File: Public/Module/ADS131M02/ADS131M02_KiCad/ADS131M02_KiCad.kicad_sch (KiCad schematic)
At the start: 8 parts, among them U1 ADS131M02_TSSOP20, U2 LP2985-3.3

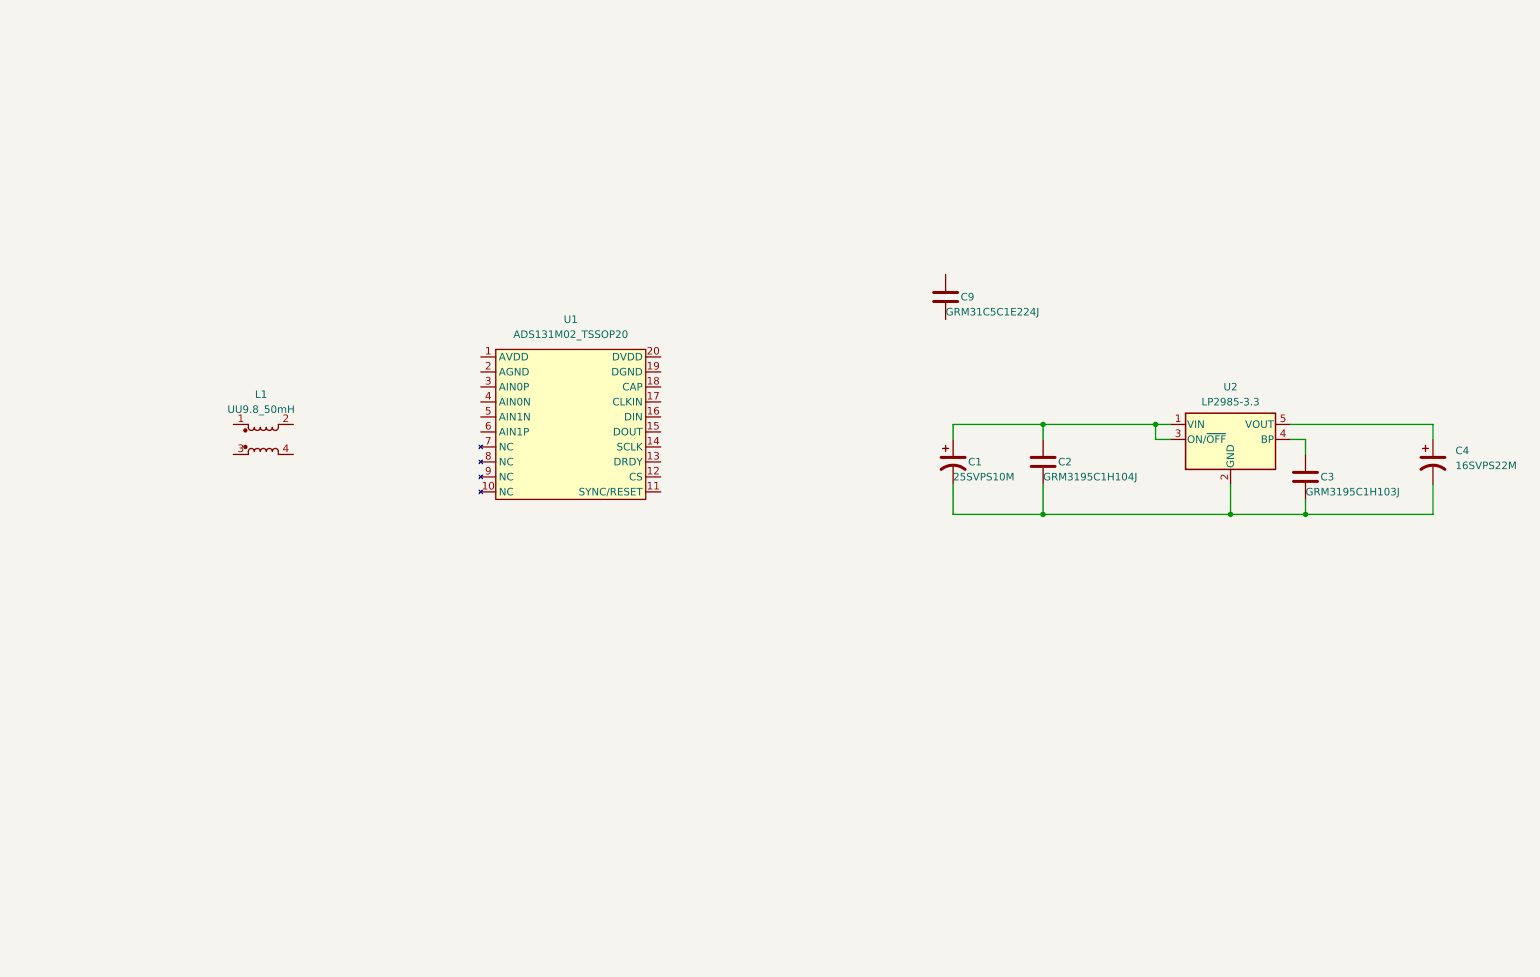
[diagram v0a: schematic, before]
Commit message: Update ADS131M02 Module
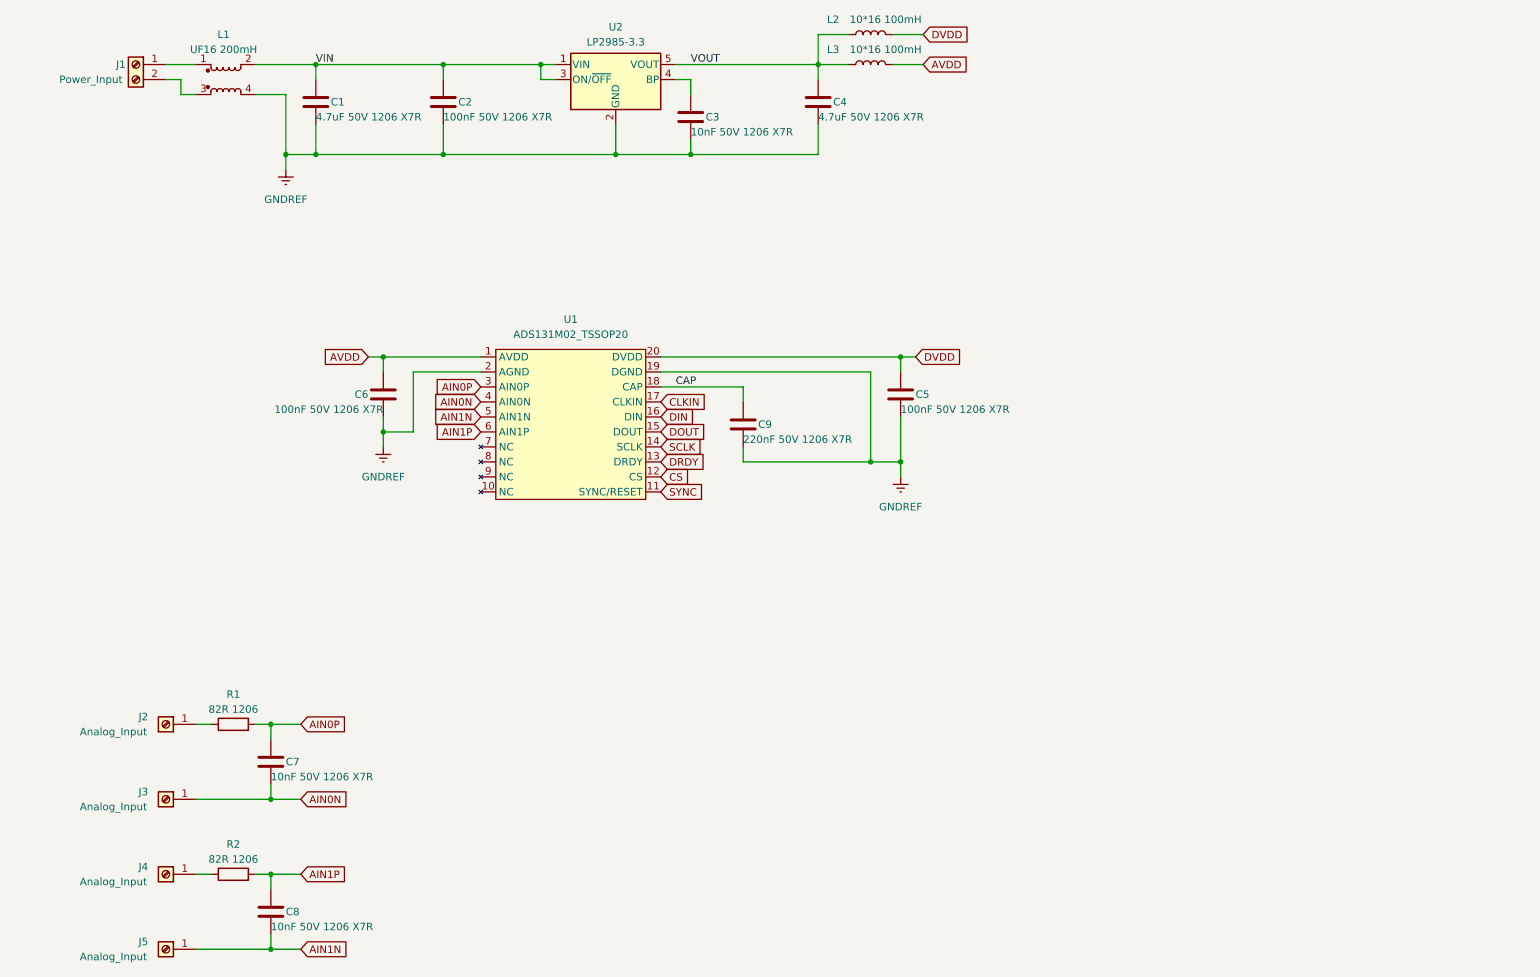
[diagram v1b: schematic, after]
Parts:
- removed C1: 25SVPS10M, symbol Device:C_Polarized_US
- removed C4: 16SVPS22M, symbol Device:C_Polarized_US
- added C1, C4: 4.7uF 50V 1206 X7R, Capacitor_SMD:C_1206_3216Metric, symbol Device:C
- added C5, C6: 100nF 50V 1206 X7R, Capacitor_SMD:C_1206_3216Metric, symbol Device:C
- added C7, C8: 10nF 50V 1206 X7R, Capacitor_SMD:C_1206_3216Metric, symbol Device:C
- added J1: Power_Input, Customer_Connector:2EDG-5.08mm_2P_Horizontal, symbol Connector:Screw_Terminal_01x02
- added J2, J3, J4, J5: Analog_Input, Customer_Connector:AMASS_24.245, symbol Connector:Screw_Terminal_01x01
- added L2, L3: 10*16 100mH, symbol Device:L
- added R1, R2: 82R 1206, Resistor_SMD:R_1206_3216Metric, symbol Device:R
- C2: value GRM3195C1H104J -> 100nF 50V 1206 X7R; footprint (none) -> Capacitor_SMD:C_1206_3216Metric
- C3: value GRM3195C1H103J -> 10nF 50V 1206 X7R; footprint (none) -> Capacitor_SMD:C_1206_3216Metric
- C9: value GRM31C5C1E224J -> 220nF 50V 1206 X7R; footprint (none) -> Capacitor_SMD:C_1206_3216Metric
- L1: value UU9.8_50mH -> UF16 200mH
- U1: footprint (none) -> Package_SO:TSSOP-20_4.4x6.5mm_P0.65mm
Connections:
- net VIN: now reaches C2.1, U2.1 (VIN), U2.3 (ON/~{OFF})
- net VIN: now also L1.2, C1.1
- net GNDREF: now reaches C2.2, C3.2, U2.2 (GND)
- net GNDREF: now also C9.2, L1.4, U1.19 (DGND), U1.2 (AGND), C1.2, C4.2, C5.2, C6.2
- net VOUT: now reaches U2.5 (VOUT)
- net VOUT: now also C4.1, L2.1, L3.1
- net at L1.1: now also J1.1 (Pin_1)
- net at L1.3: now also J1.2 (Pin_2)
- net AVDD: now reaches U1.1 (AVDD)
- net AVDD: now also C6.1, L3.2
- net SYNC: now reaches U1.11 (SYNC/RESET)
- net CS: now reaches U1.12 (CS)
- net DRDY: now reaches U1.13 (DRDY)
- net SCLK: now reaches U1.14 (SCLK)
- net DOUT: now reaches U1.15 (DOUT)
- net DIN: now reaches U1.16 (DIN)
- net CLKIN: now reaches U1.17 (CLKIN)
- net CAP: now reaches U1.18 (CAP)
- net CAP: now also C9.1
- net DVDD: now reaches U1.20 (DVDD)
- net DVDD: now also C5.1, L2.2
- net AIN0P: now reaches U1.3 (AIN0P)
- net AIN0P: now also C7.1, R1.2
- net AIN0N: now reaches U1.4 (AIN0N)
- net AIN0N: now also C7.2, J3.1 (Pin_1)
- net AIN1N: now reaches U1.5 (AIN1N)
- net AIN1N: now also C8.2, J5.1 (Pin_1)
- net AIN1P: now reaches U1.6 (AIN1P)
- net AIN1P: now also C8.1, R2.2
- new net: J2.1 (Pin_1), R1.1
- new net: J4.1 (Pin_1), R2.1
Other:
- moved on the sheet: C2, C3, C9, L1, U2

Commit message: Update ADS131M02 Module
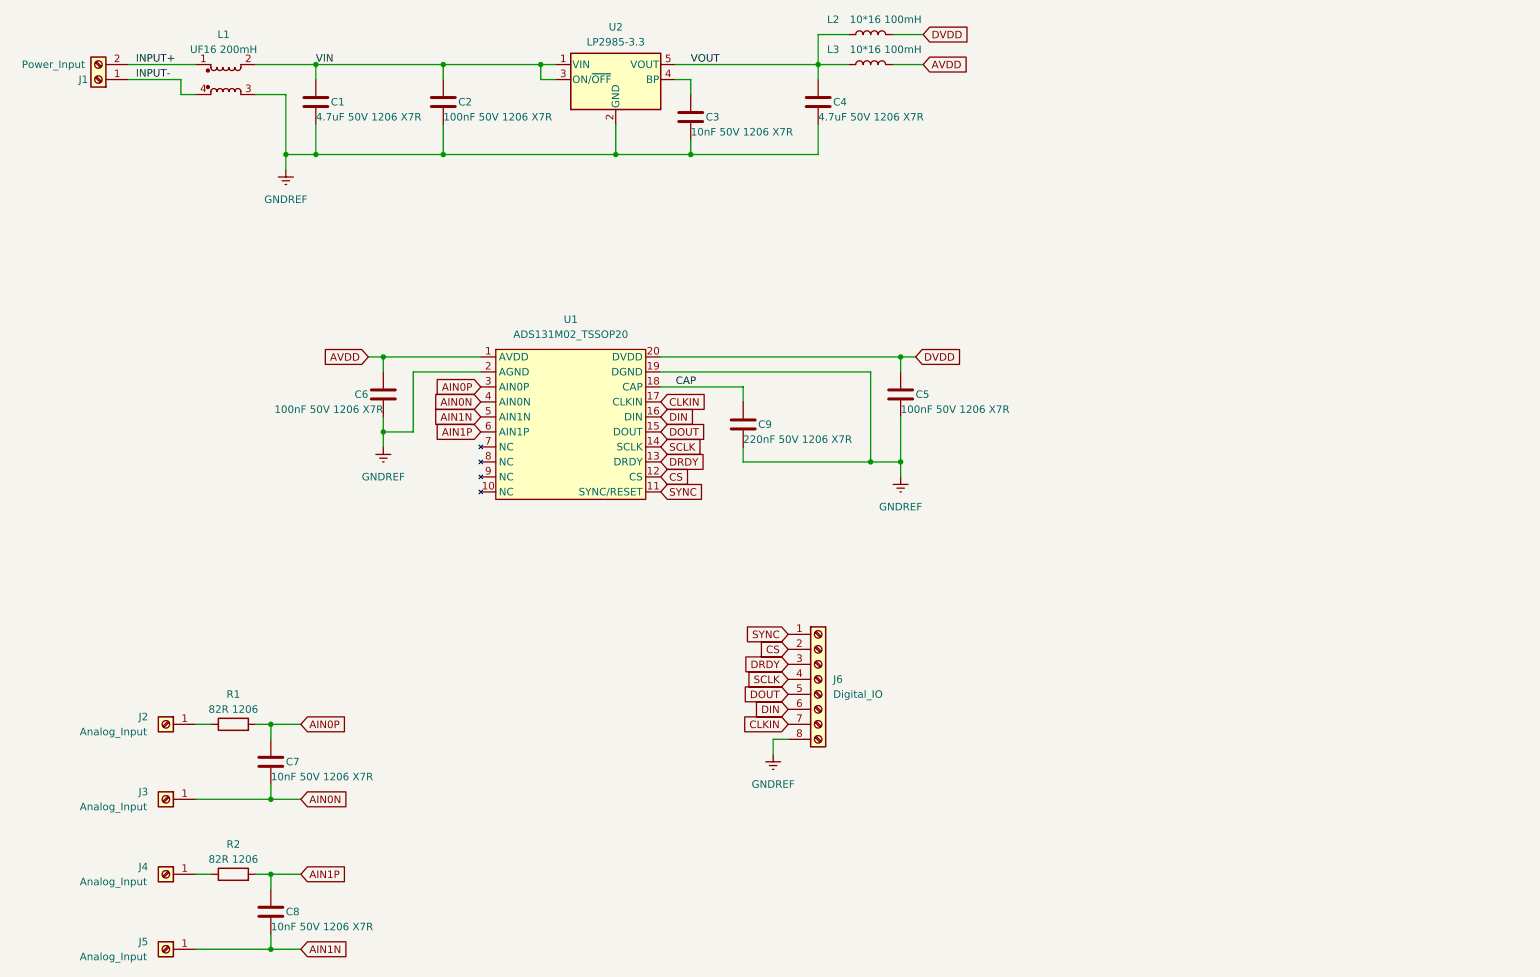
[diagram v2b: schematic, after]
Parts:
- added J6: Digital_IO, Customer_Connector:2EDG-5.08mm_8P_Horizontal, symbol Connector:Screw_Terminal_01x08
- L1: footprint (none) -> Customer_Passive:Inductor_Coupled_THT_UF16; symbol Device:L_Coupled -> Device:L_Coupled_1243
- L2, L3: footprint (none) -> Customer_Passive:Inductor_THT_10x16
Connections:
- net CLKIN: now also J6.7 (Pin_7)
- net CS: now also J6.2 (Pin_2)
- net DIN: now also J6.6 (Pin_6)
- net DOUT: now also J6.5 (Pin_5)
- net DRDY: now also J6.3 (Pin_3)
- net GNDREF: now also L1.3, J6.8 (Pin_8); no longer L1.4
- net SCLK: now also J6.4 (Pin_4)
- net SYNC: now also J6.1 (Pin_1)
- net INPUT+: now reaches L1.1
- net INPUT+: now also J1.2 (Pin_2); no longer J1.1 (Pin_1)
- new net INPUT-: J1.1 (Pin_1), L1.4
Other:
- moved on the sheet: J1
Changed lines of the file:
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@@
+    (stroke (width 0) (type default))
+  )
+  (wire (pts (xy 148.59 144.78) (xy 148.59 142.24))
     (stroke (width 0) (type default))
   )
@@
     (stroke (width 0) (type default))
   )
-  (wire (pts (xy 45.72 27.94) (xy 50.8 27.94))
+  (wire (pts (xy 39.37 27.94) (xy 50.8 27.94))
     (stroke (width 0) (type default))
   )
@@
     (stroke (width 0) (type default))
   )
+  (wire (pts (xy 148.59 142.24) (xy 151.13 142.24))
+    (stroke (width 0) (type default))
+  )
   (wire (pts (xy 143.51 92.71) (xy 143.51 95.25))
     (stroke (width 0) (type default))
@@
     (stroke (width 0) (type default))
   )
-  (wire (pts (xy 45.72 30.48) (xy 48.26 30.48))
+  (wire (pts (xy 39.37 30.48) (xy 48.26 30.48))
     (stroke (width 0) (type default))
   )
@@
   (wire (pts (xy 92.71 43.18) (xy 121.92 43.18))
     (stroke (width 0) (type default))
+  )
+  (label "INPUT-" (at 40.64 30.48 0) (fields_autoplaced)
+    (effects (font (size 1.27 1.27)) (justify left bottom))
   )
   (label "CAP" (at 132.08 82.55 0) (fields_autoplaced)
     (effects (font (size 1.27 1.27)) (justify left bottom))
   )
+  (label "INPUT+" (at 40.64 27.94 0) (fields_autoplaced)
+    (effects (font (size 1.27 1.27)) (justify left bottom))
+  )
   (label "VOUT" (at 134.62 27.94 0) (fields_autoplaced)
     (effects (font (size 1.27 1.27)) (justify left bottom))
@@
     )
   )
+  (global_label "DRDY" (shape input) (at 151.13 129.54 180) (fields_autoplaced)
+    (effects (font (size 1.27 1.27)) (justify right))
+    (property "Intersheetrefs" "${INTERSHEET_REFS}" (at 143.2462 129.54 0)
+      (effects (font (size 1.27 1.27)) (justify right) hide)
+    )
+  )
   (global_label "DVDD" (shape input) (at 173.99 22.86 0) (fields_autoplaced)
     (effects (font (size 1.27 1.27)) (justify left))
@@
     )
   )
+  (global_label "SCLK" (shape input) (at 151.13 132.08 180) (fields_autoplaced)
+    (effects (font (size 1.27 1.27)) (justify right))
+    (property "Intersheetrefs" "${INTERSHEET_REFS}" (at 143.3672 132.08 0)
+      (effects (font (size 1.27 1.27)) (justify right) hide)
+    )
+  )
   (global_label "AIN1P" (shape input) (at 68.58 165.1 0) (fields_autoplaced)
     (effects (font (size 1.27 1.27)) (justify left))
@@
     )
   )
+  (global_label "CS" (shape input) (at 151.13 127 180) (fields_autoplaced)
+    (effects (font (size 1.27 1.27)) (justify right))
+    (property "Intersheetrefs" "${INTERSHEET_REFS}" (at 145.6653 127 0)
+      (effects (font (size 1.27 1.27)) (justify right) hide)
+    )
+  )
   (global_label "CLKIN" (shape input) (at 129.54 85.09 0) (fields_autoplaced)
     (effects (font (size 1.27 1.27)) (justify left))
@@
     )
   )
+  (global_label "DIN" (shape input) (at 151.13 137.16 180) (fields_autoplaced)
+    (effects (font (size 1.27 1.27)) (justify right))
+    (property "Intersheetrefs" "${INTERSHEET_REFS}" (at 144.9395 137.16 0)
+      (effects (font (size 1.27 1.27)) (justify right) hide)
+    )
+  )
+  (global_label "DOUT" (shape input) (at 151.13 134.62 180) (fields_autoplaced)
+    (effects (font (size 1.27 1.27)) (justify right))
+    (property "Intersheetrefs" "${INTERSHEET_REFS}" (at 143.2462 134.62 0)
+      (effects (font (size 1.27 1.27)) (justify right) hide)
+    )
+  )
+  (global_label "SYNC" (shape input) (at 151.13 124.46 180) (fields_autoplaced)
+    (effects (font (size 1.27 1.27)) (justify right))
+    (property "Intersheetrefs" "${INTERSHEET_REFS}" (at 143.2462 124.46 0)
+      (effects (font (size 1.27 1.27)) (justify right) hide)
+    )
+  )
   (global_label "DVDD" (shape input) (at 172.72 77.47 0) (fields_autoplaced)
     (effects (font (size 1.27 1.27)) (justify left))
@@
     )
   )
+  (global_label "CLKIN" (shape input) (at 151.13 139.7 180) (fields_autoplaced)
+    (effects (font (size 1.27 1.27)) (justify right))
+    (property "Intersheetrefs" "${INTERSHEET_REFS}" (at 142.6414 139.7 0)
+      (effects (font (size 1.27 1.27)) (justify right) hide)
+    )
+  )
   (symbol (lib_id "Connector:Screw_Terminal_01x01") (at 45.72 177.8 0) (mirror y) (unit 1)
     (in_bom yes) (on_board yes) (dnp no)
@@
       (effects (font (size 1.27 1.27)))
     )
-    (property "Footprint" "" (at 165.1 22.86 0)
+    (property "Footprint" "Customer_Passive:Inductor_THT_10x16" (at 165.1 22.86 0)
       (effects (font (size 1.27 1.27)) hide)
     )
@@
     )
   )
-  (symbol (lib_id "Connector:Screw_Terminal_01x02") (at 40.64 27.94 0) (mirror y) (unit 1)
-    (in_bom yes) (on_board yes) (dnp no)
-    (property "Reference" "J1" (at 38.1 27.94 0)
-      (effects (font (size 1.27 1.27)))
-    )
-    (property "Value" "Power_Input" (at 33.02 30.48 0)
-      (effects (font (size 1.27 1.27)))
-    )
-    (property "Footprint" "Customer_Connector:2EDG-5.08mm_2P_Horizontal" (at 40.64 27.94 0)
-      (effects (font (size 1.27 1.27)) hide)
-    )
-    (property "Datasheet" "~" (at 40.64 27.94 0)
+  (symbol (lib_id "Connector:Screw_Terminal_01x02") (at 34.29 30.48 180) (unit 1)
+    (in_bom yes) (on_board yes) (dnp no)
+    (property "Reference" "J1" (at 31.75 30.48 0)
+      (effects (font (size 1.27 1.27)))
+    )
+    (property "Value" "Power_Input" (at 26.67 27.94 0)
+      (effects (font (size 1.27 1.27)))
+    )
+    (property "Footprint" "Customer_Connector:2EDG-5.08mm_2P_Horizontal" (at 34.29 30.48 0)
+      (effects (font (size 1.27 1.27)) hide)
+    )
+    (property "Datasheet" "~" (at 34.29 30.48 0)
       (effects (font (size 1.27 1.27)) hide)
     )
@@
     )
   )
-  (symbol (lib_id "Device:L_Coupled") (at 55.88 30.48 0) (unit 1)
-    (in_bom yes) (on_board yes) (dnp no) (fields_autoplaced)
+  (symbol (lib_id "Device:L_Coupled_1243") (at 55.88 30.48 0) (unit 1)
+    (in_bom yes) (on_board yes) (dnp no)
     (property "Reference" "L1" (at 55.499 22.86 0)
       (effects (font (size 1.27 1.27)))
@@
       (effects (font (size 1.27 1.27)))
     )
-    (property "Footprint" "" (at 55.88 30.48 0)
+    (property "Footprint" "Customer_Passive:Inductor_Coupled_THT_UF16" (at 55.88 30.48 0)
       (effects (font (size 1.27 1.27)) hide)
     )
@@
     )
   )
+  (symbol (lib_id "Connector:Screw_Terminal_01x08") (at 156.21 132.08 0) (unit 1)
+    (in_bom yes) (on_board yes) (dnp no) (fields_autoplaced)
+    (property "Reference" "J6" (at 158.75 132.08 0)
+      (effects (font (size 1.27 1.27)) (justify left))
+    )
+    (property "Value" "Digital_IO" (at 158.75 134.62 0)
+      (effects (font (size 1.27 1.27)) (justify left))
+    )
+    (property "Footprint" "Customer_Connector:2EDG-5.08mm_8P_Horizontal" (at 156.21 132.08 0)
+      (effects (font (size 1.27 1.27)) hide)
+    )
+    (property "Datasheet" "~" (at 156.21 132.08 0)
+      (effects (font (size 1.27 1.27)) hide)
+    )
+    (pin "1")
+    (pin "2")
+    (pin "3")
+    (pin "4")
+    (pin "5")
+    (pin "6")
+    (pin "7")
+    (pin "8")
+    (instances
+      (project "ADS131M02_KiCad"
+        (path "/7d2fbb59-57e0-429a-94f3-b0f859024267"
+          (reference "J6") (unit 1)
+        )
+      )
+    )
+  )
   (symbol (lib_id "Device:C") (at 143.51 88.9 0) (unit 1)
     (in_bom yes) (on_board yes) (dnp no)
@@
       (effects (font (size 1.27 1.27)))
     )
-    (property "Footprint" "" (at 165.1 27.94 0)
+    (property "Footprint" "Customer_Passive:Inductor_THT_10x16" (at 165.1 27.94 0)
       (effects (font (size 1.27 1.27)) hide)
     )
@@
         )
       )
+    )
+  )
+  (symbol (lib_id "power:GNDREF") (at 148.59 144.78 0) (unit 1)
+    (in_bom yes) (on_board yes) (dnp no) (fields_autoplaced)
+    (property "Reference" "#PWR04" (at 148.59 151.13 0)
+      (effects (font (size 1.27 1.27)) hide)
+    )
+    (property "Value" "GNDREF" (at 148.59 149.86 0)
+      (effects (font (size 1.27 1.27)))
+    )
+    (property "Footprint" "" (at 148.59 144.78 0)
+      (effects (font (size 1.27 1.27)) hide)
+    )
+    (property "Datasheet" "" (at 148.59 144.78 0)
+      (effects (font (size 1.27 1.27)) hide)
+    )
+    (pin "1")
+    (instances
+      (project "ADS131M02_KiCad"
+        (path "/7d2fbb59-57e0-429a-94f3-b0f859024267"
+          (reference "#PWR04") (unit 1)
+        )
+      )
